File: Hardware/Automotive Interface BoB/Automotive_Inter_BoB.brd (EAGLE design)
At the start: 25.4 x 25.4 mm, 49 parts, among them U1 HCPL-270L

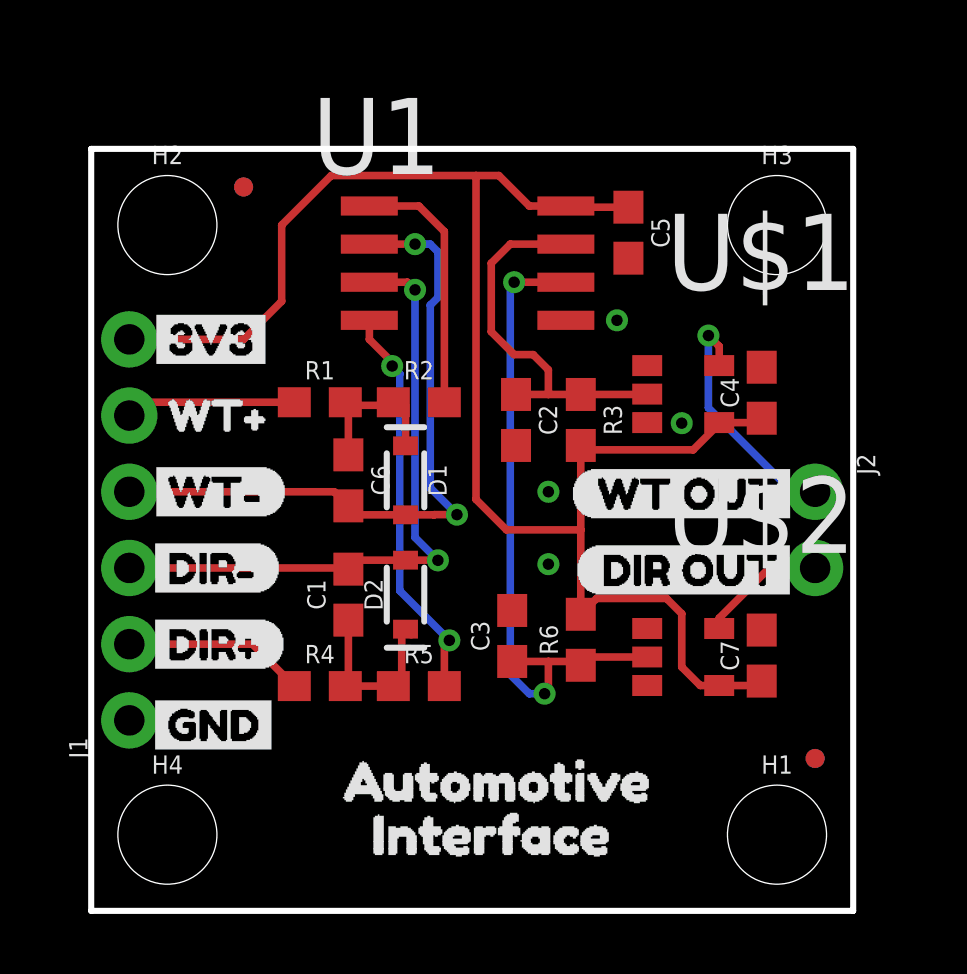
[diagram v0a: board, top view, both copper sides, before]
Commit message: Updates the optocoupler in the Automotive breakout
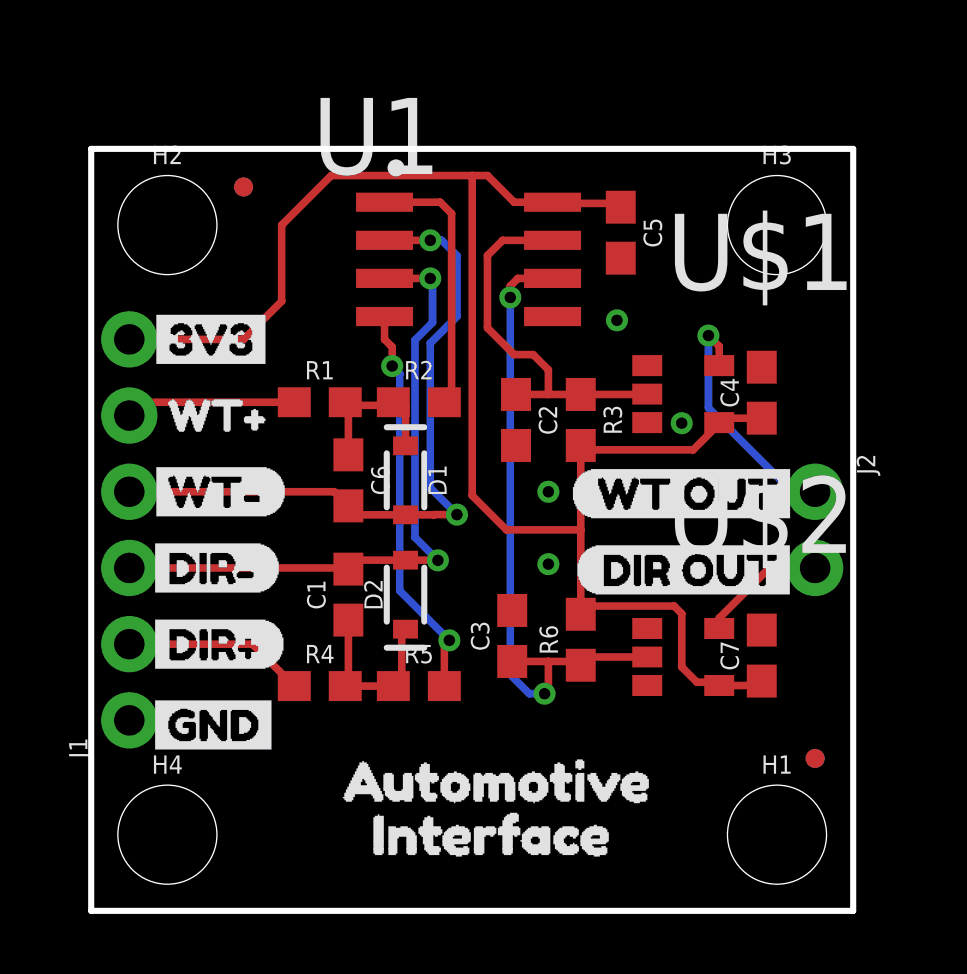
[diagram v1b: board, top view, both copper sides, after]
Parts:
- moved C5 0.25 mm to (17.7, 22.6)
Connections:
- net DIR_U-BLOX renamed DIR_OUT
- net WT_U-BLOX renamed WT_OUT
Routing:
- net DIR-: track 21.4 -> 21.9 mm
